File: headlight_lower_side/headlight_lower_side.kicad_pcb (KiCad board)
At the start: 2 copper layers, 78.5 x 73 mm, 22 parts, among them J1 Conn_01x06_Pin, J2 Conn_02x03_Odd_Even

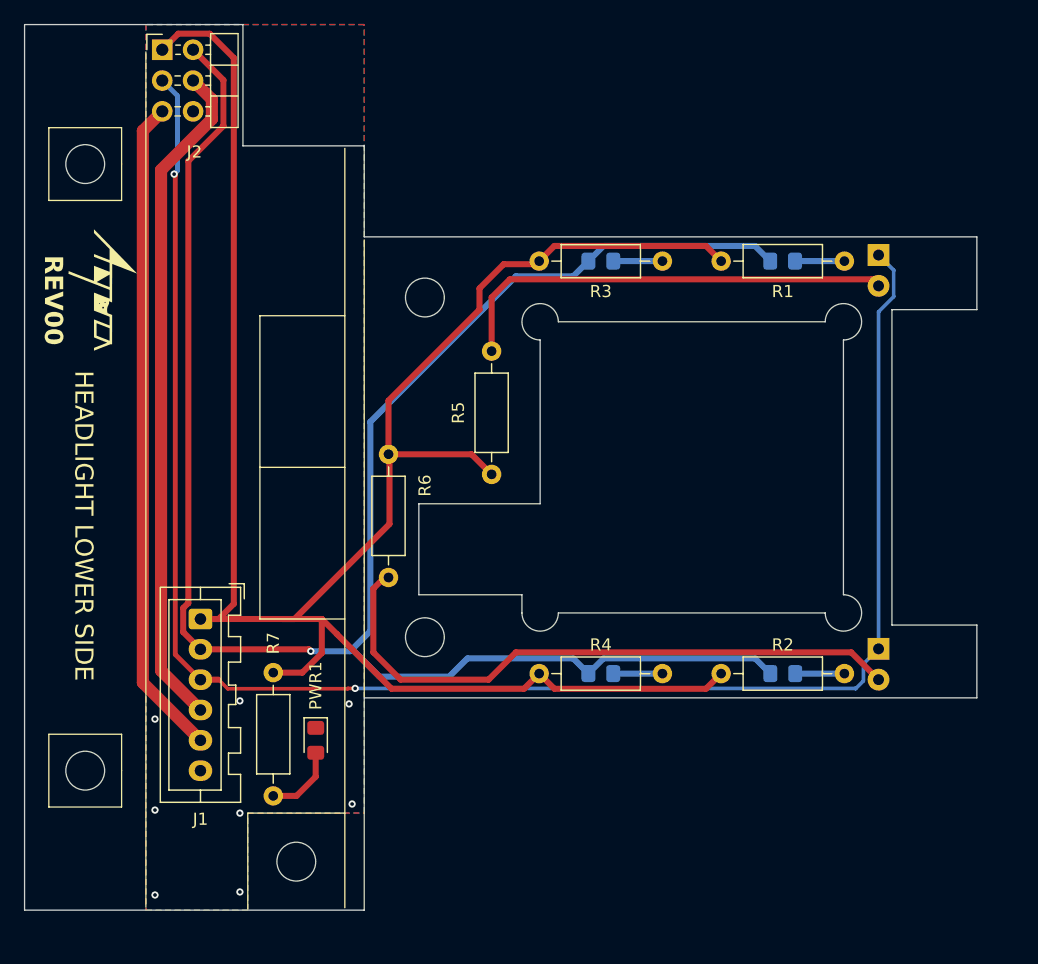
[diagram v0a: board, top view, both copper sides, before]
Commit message: 基板防水REV00発注完了
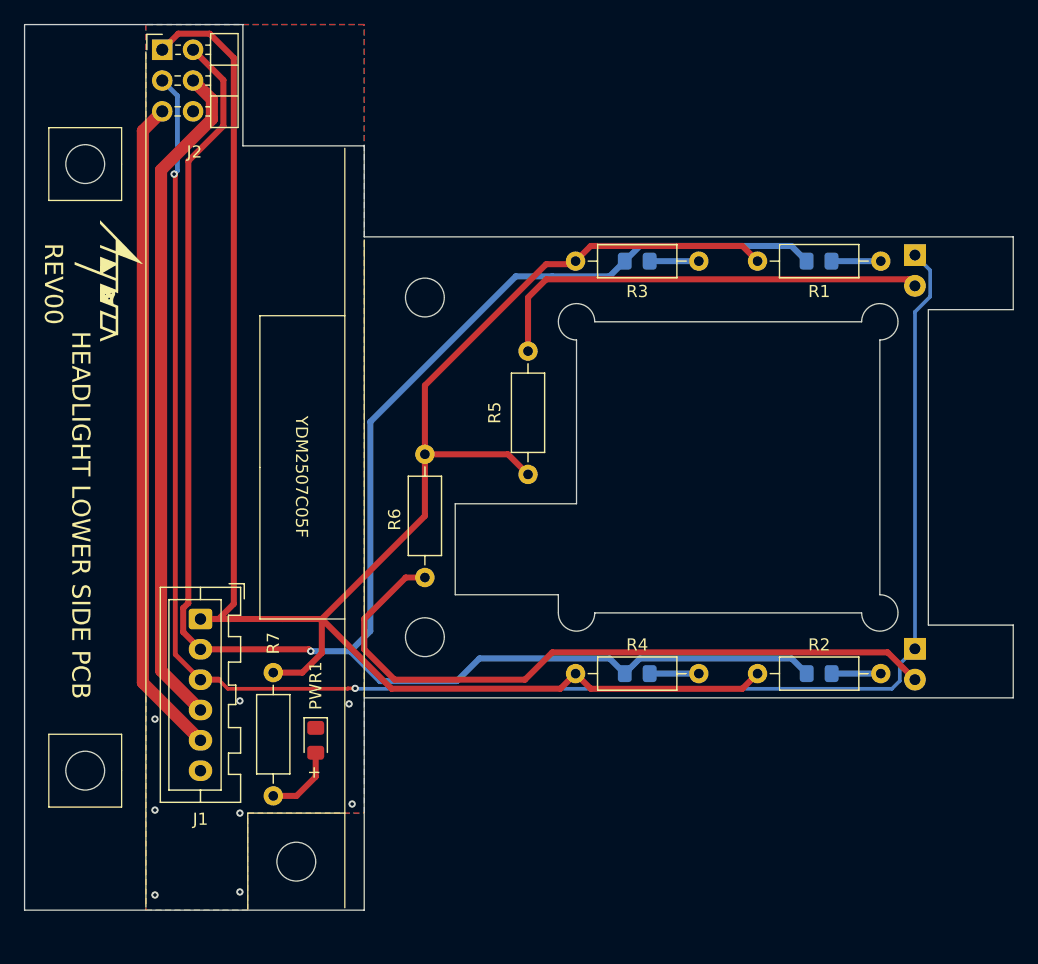
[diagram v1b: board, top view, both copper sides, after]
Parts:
- R1, R2, R3, R4: value 200 -> 180
- R5, R6: value 200 -> 100
- R7: value 200 -> 750
- moved IR1 3.00 mm to (109.9, 44.5)
- moved IR2 3.00 mm to (109.9, 77.0)
- moved LB1 3.00 mm to (102.0, 45.0)
- moved LB2 3.00 mm to (102.0, 79.0)
- moved LB3 3.00 mm to (87.0, 45.0)
- moved LB4 3.00 mm to (87.0, 79.0)
- moved R1 3.00 mm to (96.9, 45.0)
- moved R2 3.00 mm to (96.9, 79.0)
- moved R3 3.00 mm to (81.9, 45.0)
- moved R4 3.00 mm to (81.9, 79.0)
- moved R5 3.00 mm to (78.0, 62.6)
- moved R6 3.00 mm to (69.5, 60.9)
- moved G*** 0.90 mm to (43.5, 46.5)
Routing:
- net LB: track 161.5 -> 167.9 mm
- net Net-(IR2-A): track 51.3 -> 57.2 mm
- net IR: track 141.8 -> 144.8 mm
- net +5.1V: track 175.6 -> 177.6 mm
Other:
- board size 78.5 x 73 mm -> 81.5 x 73 mm
- board text added: "+"
- board text added: "HEADLIGHT LOWER SIDE PCB"
- board text added: "YDM2507C05F"
- board text removed: "HEADLIGHT LOWER SIDE"

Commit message: ヘッドライト基盤REV01作成
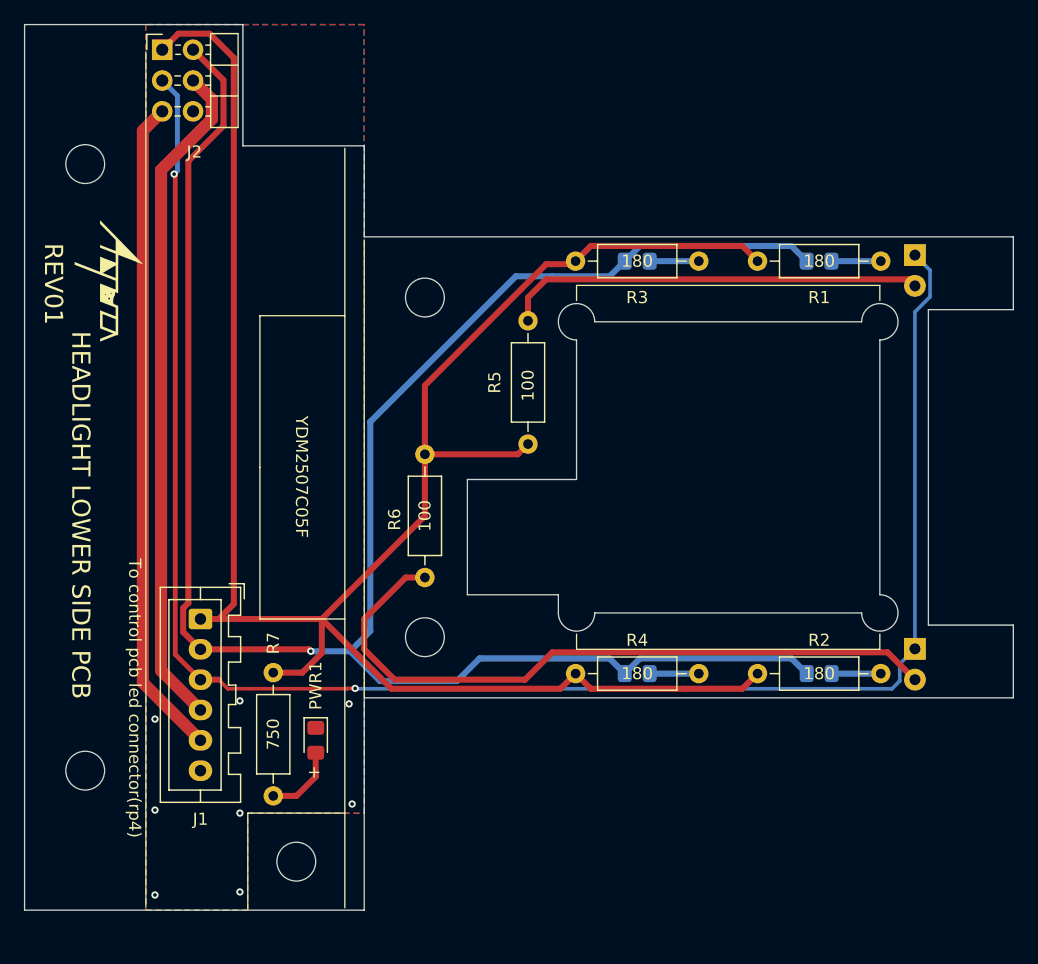
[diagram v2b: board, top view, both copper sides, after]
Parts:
- moved R5 2.50 mm to (78.0, 60.1)
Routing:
- net Net-(IR1-A): track 37.2 -> 34.7 mm
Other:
- outline, holes or cut-outs redrawn
- board text added: "REV01"
- board text added: "To control pcb led connector(rp4)"
- board text removed: "REV00"
